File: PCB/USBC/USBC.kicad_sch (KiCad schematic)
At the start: 27 parts, among them J1 USB-C-Plug-V, J2 Shelly, J3 USB-PROG, U2 ESP32-S3-MINI-1, U2 SCD41, U5 MD8942

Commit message: Tidy
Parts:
- U2: value SCD41 -> SCD41-D-R1
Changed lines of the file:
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@@
   (junction (at 66.675 70.485) (diameter 0) (color 0 0 0 0)
   )
-  (junction (at 205.105 77.47) (diameter 0) (color 0 0 0 0)
-  )
   (junction (at 124.46 57.785) (diameter 0) (color 0 0 0 0)
   )
@@
   )
   (junction (at 178.435 77.47) (diameter 0) (color 0 0 0 0)
-  )
-  (junction (at 206.375 39.37) (diameter 0) (color 0 0 0 0)
   )
   (junction (at 170.815 93.345) (diameter 0) (color 0 0 0 0)
@@
     (stroke (width 0) (type default))
   )
-  (wire (pts (xy 206.375 39.37) (xy 198.755 39.37))
+  (wire (pts (xy 198.755 39.37) (xy 210.185 39.37))
     (stroke (width 0) (type default))
   )
@@
     (stroke (width 0) (type default))
   )
-  (wire (pts (xy 208.915 77.47) (xy 205.105 77.47))
-    (stroke (width 0) (type default))
-  )
   (wire (pts (xy 152.4 100.965) (xy 156.21 100.965))
     (stroke (width 0) (type default))
@@
     (stroke (width 0) (type default))
   )
-  (wire (pts (xy 178.435 77.47) (xy 205.105 77.47))
-    (stroke (width 0) (type default))
-  )
-  (wire (pts (xy 210.185 39.37) (xy 206.375 39.37))
+  (wire (pts (xy 178.435 77.47) (xy 208.915 77.47))
     (stroke (width 0) (type default))
   )
@@
       (effects (font (size 1.27 1.27)) (justify left))
     )
-    (property "Value" "SCD41" (at 75.565 60.7572 0)
+    (property "Value" "SCD41-D-R1" (at 75.565 60.7572 0)
       (effects (font (size 1.27 1.27)) (justify left))
     )
@@
         (path "/2d210a96-f81f-42a9-8bf4-1b43c11086f3"
           (reference "#PWR06") (unit 1)
-        )
-      )
-    )
-  )
-  (symbol (lib_id "power:PWR_FLAG") (at 205.105 77.47 0) (unit 1)
-    (in_bom yes) (on_board yes) (dnp no) (fields_autoplaced)
-    (property "Reference" "#FLG02" (at 205.105 75.565 0)
-      (effects (font (size 1.27 1.27)) hide)
-    )
-    (property "Value" "PWR_FLAG" (at 205.105 73.3369 0)
-      (effects (font (size 1.27 1.27)))
-    )
-    (property "Footprint" "" (at 205.105 77.47 0)
-      (effects (font (size 1.27 1.27)) hide)
-    )
-    (property "Datasheet" "~" (at 205.105 77.47 0)
-      (effects (font (size 1.27 1.27)) hide)
-    )
-    (pin "1")
-    (instances
-      (project "USBC"
-        (path "/2d210a96-f81f-42a9-8bf4-1b43c11086f3"
-          (reference "#FLG02") (unit 1)
         )
       )
@@
         )
       )
-    )
-  )
-  (symbol (lib_id "power:PWR_FLAG") (at 206.375 39.37 0) (unit 1)
-    (in_bom yes) (on_board yes) (dnp no) (fields_autoplaced)
-    (property "Reference" "#FLG01" (at 206.375 37.465 0)
-      (effects (font (size 1.27 1.27)) hide)
-    )
-    (property "Value" "PWR_FLAG" (at 206.375 35.2369 0)
-      (effects (font (size 1.27 1.27)))
-    )
-    (property "Footprint" "" (at 206.375 39.37 0)
-      (effects (font (size 1.27 1.27)) hide)
-    )
-    (property "Datasheet" "~" (at 206.375 39.37 0)
-      (effects (font (size 1.27 1.27)) hide)
-    )
-    (pin "1")
-    (instances
-      (project "USBC"
-        (path "/2d210a96-f81f-42a9-8bf4-1b43c11086f3"
-          (reference "#FLG01") (unit 1)
-        )
-      )

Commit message: neater
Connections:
- net GND: no longer U2.17 (GPIO13)
- net LED: now also U2.29 (GPIO34); no longer U2.15 (GPIO11)
- net SCL: now also U2.17 (GPIO13); no longer U2.14 (GPIO10)
- net SDA: now also U2.16 (GPIO12); no longer U2.13 (GPIO9)
- no-connect marks 24 -> 25
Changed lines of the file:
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@@
   (junction (at 163.195 93.345) (diameter 0) (color 0 0 0 0)
   )
-  (no_connect (at 124.46 70.485))
+  (no_connect (at 93.98 78.105))
   (no_connect (at 193.675 46.99))
   (no_connect (at 124.46 90.805))
@@
   (no_connect (at 93.98 57.785))
   (no_connect (at 161.29 133.35))
-  (no_connect (at 93.98 80.645))
+  (no_connect (at 93.98 73.025))
+  (no_connect (at 93.98 75.565))
   (no_connect (at 124.46 83.185))
   (no_connect (at 93.98 55.245))
@@
     )
   )
-  (global_label "SCL" (shape output) (at 93.98 75.565 180) (fields_autoplaced)
-    (effects (font (size 1.27 1.27)) (justify right))
-    (property "Intersheetrefs" "${INTERSHEET_REFS}" (at 88.1414 75.565 0)
+  (global_label "SCL" (shape output) (at 93.98 83.185 180) (fields_autoplaced)
+    (effects (font (size 1.27 1.27)) (justify right))
+    (property "Intersheetrefs" "${INTERSHEET_REFS}" (at 88.1414 83.185 0)
       (effects (font (size 1.27 1.27)) (justify right) hide)
     )
@@
     )
   )
-  (global_label "LED" (shape output) (at 93.98 78.105 180) (fields_autoplaced)
-    (effects (font (size 1.27 1.27)) (justify right))
-    (property "Intersheetrefs" "${INTERSHEET_REFS}" (at 88.2019 78.105 0)
-      (effects (font (size 1.27 1.27)) (justify right) hide)
-    )
-  )
-  (global_label "SDA" (shape bidirectional) (at 93.98 73.025 180) (fields_autoplaced)
-    (effects (font (size 1.27 1.27)) (justify right))
-    (property "Intersheetrefs" "${INTERSHEET_REFS}" (at 87.1284 73.025 0)
+  (global_label "LED" (shape output) (at 124.46 70.485 0) (fields_autoplaced)
+    (effects (font (size 1.27 1.27)) (justify left))
+    (property "Intersheetrefs" "${INTERSHEET_REFS}" (at 130.2381 70.485 0)
+      (effects (font (size 1.27 1.27)) (justify left) hide)
+    )
+  )
+  (global_label "SDA" (shape bidirectional) (at 93.98 80.645 180) (fields_autoplaced)
+    (effects (font (size 1.27 1.27)) (justify right))
+    (property "Intersheetrefs" "${INTERSHEET_REFS}" (at 87.1284 80.645 0)
       (effects (font (size 1.27 1.27)) (justify right) hide)
     )
@@
         )
       )
-    )
-  )
-  (symbol (lib_id "power:GND") (at 93.98 83.185 270) (unit 1)
-    (in_bom yes) (on_board yes) (dnp no) (fields_autoplaced)
-    (property "Reference" "#PWR04" (at 87.63 83.185 0)
-      (effects (font (size 1.27 1.27)) hide)
-    )
-    (property "Value" "GND" (at 90.8051 83.185 90)
-      (effects (font (size 1.27 1.27)) (justify right))
-    )
-    (property "Footprint" "" (at 93.98 83.185 0)
-      (effects (font (size 1.27 1.27)) hide)
-    )
-    (property "Datasheet" "" (at 93.98 83.185 0)
-      (effects (font (size 1.27 1.27)) hide)
-    )
-    (pin "1")
-    (instances
-      (project "USBC"
-        (path "/2d210a96-f81f-42a9-8bf4-1b43c11086f3"
-          (reference "#PWR04") (unit 1)
-        )
-      )

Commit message: Tidy
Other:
- moved on the sheet: C4, C5, D1, D2, D3

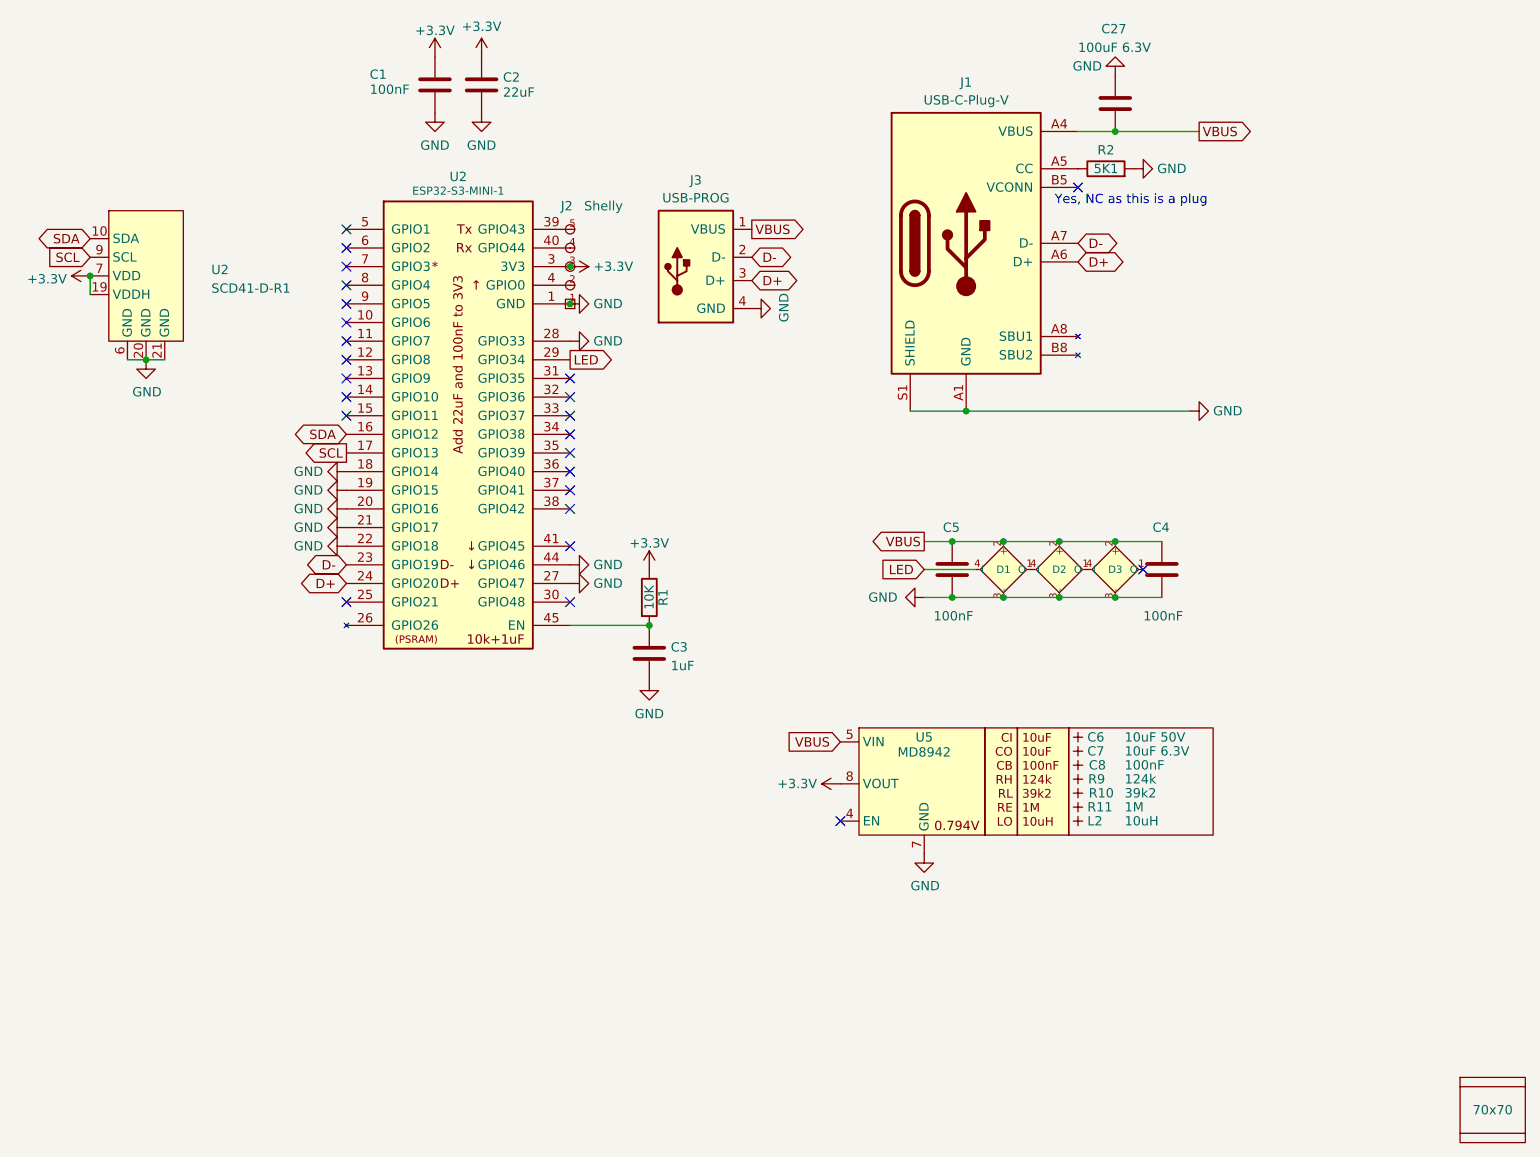
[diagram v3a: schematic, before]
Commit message: More LEDs
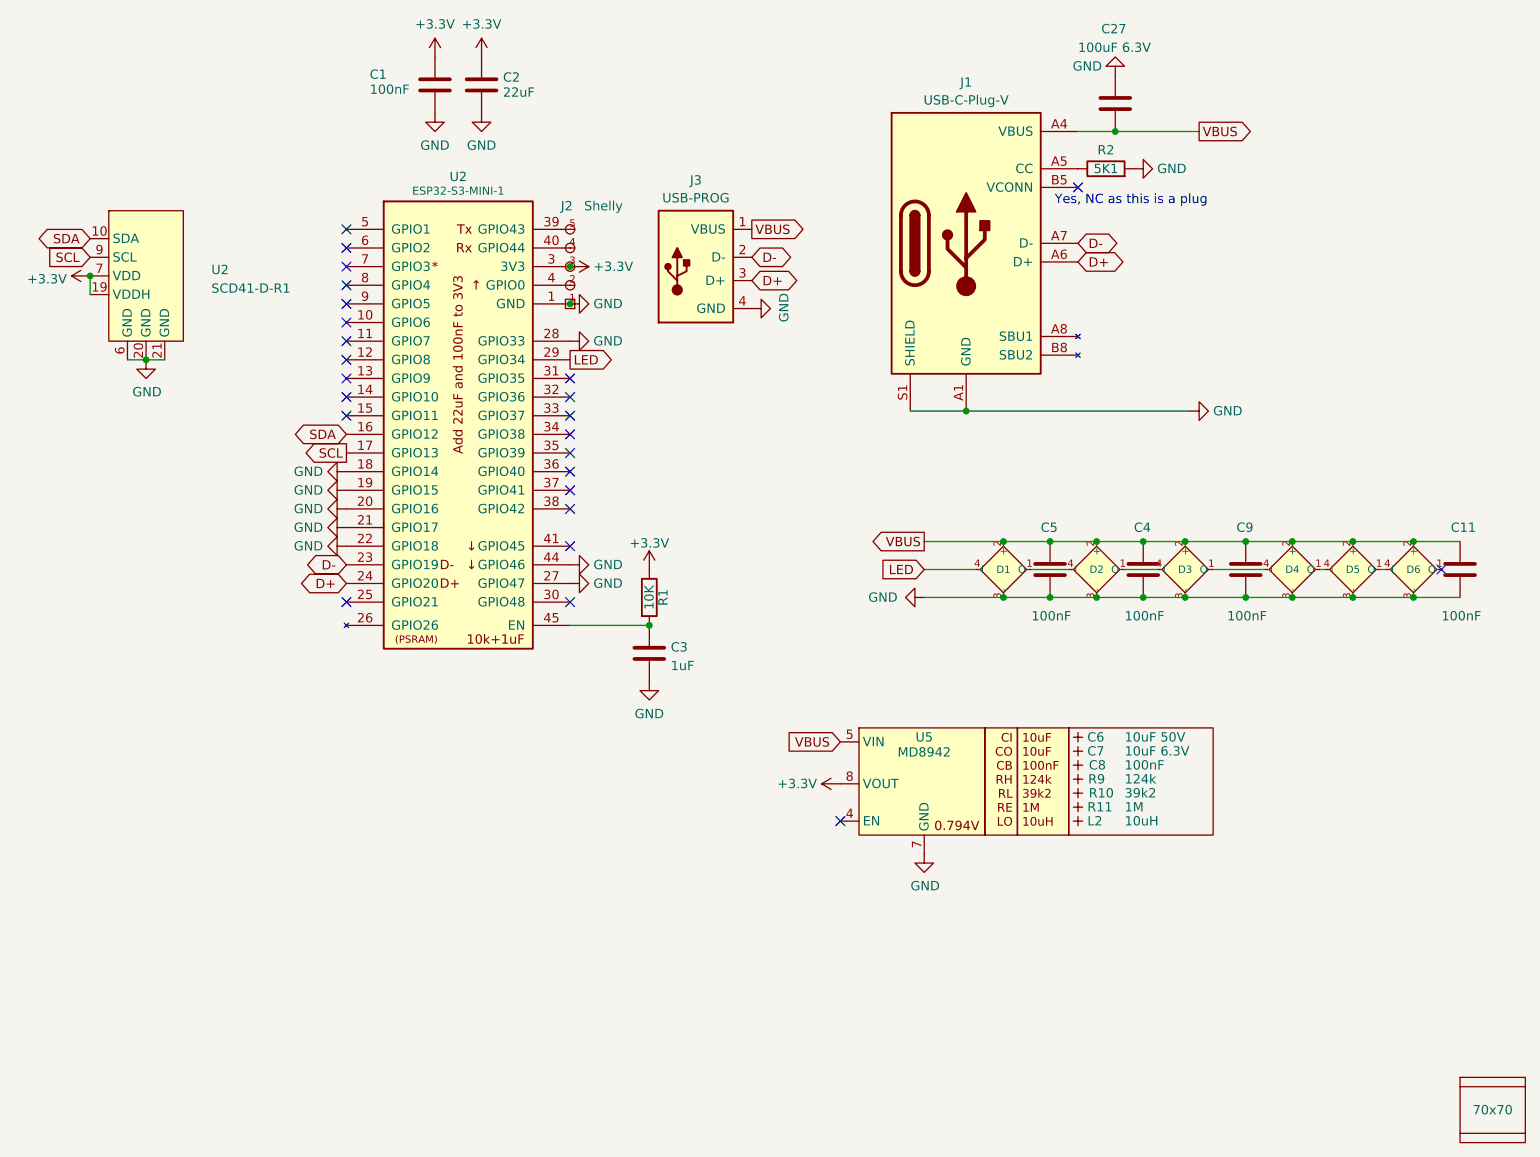
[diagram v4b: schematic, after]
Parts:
- added C11, C9: 100nF, RevK:C_0402, symbol Device:C
- added D4, D5, D6: XL-1010RGBC-WS2812B, RevK:SMD1010, symbol RevK:WS2812B-1mm
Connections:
- net GND: now also C11.2, C9.2, D4.3 (-), D5.3 (-), D6.3 (-)
- net VBUS: now also C11.1, C9.1, D4.2 (+), D5.2 (+), D6.2 (+)
- net at D3.1 (O): now also D4.4 (I)
- new net: D5.1 (O), D6.4 (I)
- new net: D4.1 (O), D5.4 (I)
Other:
- moved on the sheet: C4, C5, D2, D3

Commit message: Tody
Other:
- moved on the sheet: C4, C5, D2, D3

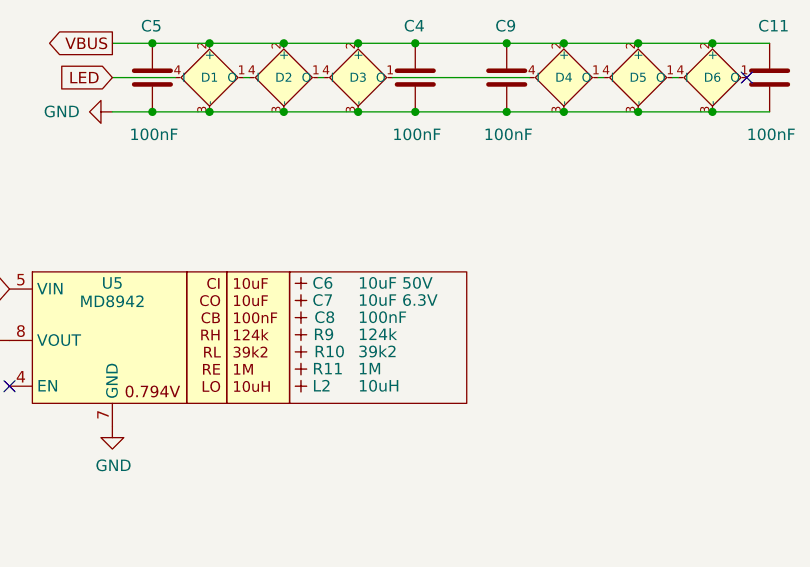
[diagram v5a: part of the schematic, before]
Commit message: New plugs
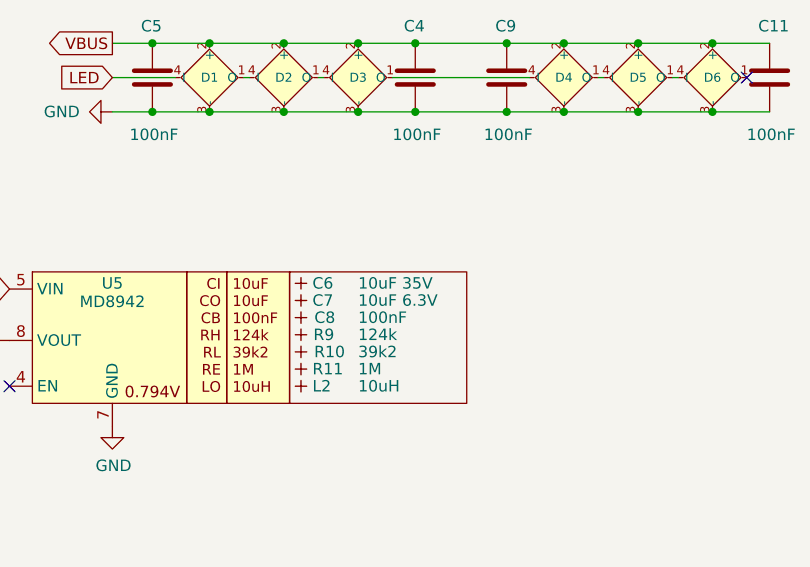
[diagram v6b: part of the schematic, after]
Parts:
- C6: value 10uF 50V -> 10uF 35V; LCSC Part # C1591 -> C194427
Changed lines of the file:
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@@
       (effects (font (size 1.27 1.27)) (justify left))
     )
-    (property "Value" "10uF 50V" (at 200.025 121.92 0)
+    (property "Value" "10uF 35V" (at 200.025 121.92 0)
       (effects (font (size 1.27 1.27)) (justify left))
     )
@@
       (effects (font (size 1.27 1.27)) hide)
     )
-    (property "LCSC Part #" "C1591" (at 193.675 121.92 0)
+    (property "LCSC Part #" "C194427" (at 193.675 121.92 0)
       (effects (font (size 1.27 1.27)) hide)
     )

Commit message: Tidy
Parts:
- removed J2: Shelly, RevK:Shelly, symbol RevK:Shelly
- removed J3: USB-PROG, RevK:USB-PROG, symbol RevK:USB-PROG
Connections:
- no-connect marks 25 -> 28

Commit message: PCB Update
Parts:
- C6: LCSC Part # C194427 -> (none); MPN (none) -> C194427
- C7: LCSC Part # C1691 -> (none); MPN (none) -> C1691
- D1, D2, D3, D4, D5, D6: LCSC Part # C5349953 -> (none); MPN (none) -> C5349953
- J1: LCSC Part # C399938 -> (none); MPN (none) -> C399938
- U2: LCSC Part # C3013941 -> (none); MPN (none) -> C3013941
- U5: LCSC Part # C2684786 -> (none); MPN (none) -> C2684786
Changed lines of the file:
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@@
 			)
 		)
-		(property "LCSC Part #" "C1691"
+		(property "MPN" "C1691"
 			(at 193.675 123.825 0)
 			(effects
@@
 			)
 		)
-		(property "LCSC Part #" "C2684786"
+		(property "MPN" "C2684786"
 			(at 172.72 154.94 0)
 			(effects
@@
 			)
 		)
-		(property "LCSC Part #" "C194427"
+		(property "MPN" "C194427"
 			(at 193.675 121.92 0)
 			(effects
@@
 			)
 		)
-		(property "LCSC Part #" "C5349953"
+		(property "MPN" "C5349953"
 			(at 184.785 87.63 0)
 			(effects
@@
 			)
 		)
-		(property "LCSC Part #" "C5349953"
+		(property "MPN" "C5349953"
 			(at 240.665 87.63 0)
 			(effects
@@
 			)
 		)
-		(property "LCSC Part #" "C399938"
+		(property "MPN" "C399938"
 			(at 178.435 54.61 0)
 			(effects
@@
 			)
 		)
-		(property "LCSC Part #" "C5349953"
+		(property "MPN" "C5349953"
 			(at 224.155 87.63 0)
 			(effects
@@
 			)
 		)
-		(property "LCSC Part #" "C5349953"
+		(property "MPN" "C5349953"
 			(at 201.295 87.63 0)
 			(effects
@@
 			)
 		)
-		(property "LCSC Part #" "C3013941"
+		(property "MPN" "C3013941"
 			(at 109.22 111.76 0)
 			(effects
@@
 			)
 		)
-		(property "LCSC Part #" "C5349953"
+		(property "MPN" "C5349953"
 			(at 232.41 87.63 0)
 			(effects
@@
 			)
 		)
-		(property "LCSC Part #" "C5349953"
+		(property "MPN" "C5349953"
 			(at 193.04 87.63 0)
 			(effects
